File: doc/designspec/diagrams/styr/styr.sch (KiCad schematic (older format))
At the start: 1 part

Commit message: Schematics done, need filters for sensors, some resistors for the switches etc
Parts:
- added U?: ATmega1284P-PU, Package_DIP:DIP-40_W15.24mm, symbol MCU_Microchip_ATmega:ATmega1284P-PU
- added U?: IQEXO-3, Package_SO:SOIC-8_3.9x4.9mm_P1.27mm, symbol exo3:IQEXO-3
- added U?: ADG419BN, Package_DIP:DIP-8_W7.62mm, symbol Analog_Switch:ADG419BN
- added _?: JMA162A, Display_7Segment:DA04-11SYKWA, symbol jma162a:JMA162A
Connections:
- net labels added: CHIP_SELECT, MISO, MOSI, PWM_MOTOR, PWM_SVÄNG, SPI_CLK
- wire segments 0 -> 51
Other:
- moved on the sheet: J?
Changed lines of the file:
@@
 EESchema Schematic File Version 4
+LIBS:styr-cache
 EELAYER 26 0
 EELAYER END
@@
 L Connector:AVR-JTAG-10 J?
 U 1 1 5BBCAF71
-P 2100 1350
-F 0 "J?" H 1720 1396 50  0000 R CNN
-F 1 "AVR-JTAG-10" H 1720 1305 50  0000 R CNN
-F 2 "" V 1950 1500 50  0001 C CNN
-F 3 " ~" H 825 800 50  0001 C CNN
-	1    2100 1350
+P 5050 3550
+F 0 "J?" H 4670 3596 50  0000 R CNN
+F 1 "AVR-JTAG-10" H 4670 3505 50  0000 R CNN
+F 2 "" V 4900 3700 50  0001 C CNN
+F 3 " ~" H 3775 3000 50  0001 C CNN
+	1    5050 3550
+	-1   0    0    -1
+$EndComp
+$Comp
+L MCU_Microchip_ATmega:ATmega1284P-PU U?
+U 1 1 5BEA84E2
+P 2850 3150
+F 0 "U?" H 2850 1064 50  0000 C CNN
+F 1 "ATmega1284P-PU" H 2850 973 50  0000 C CNN
+F 2 "Package_DIP:DIP-40_W15.24mm" H 2850 3150 50  0001 C CIN
+F 3 "http://ww1.microchip.com/downloads/en/DeviceDoc/Atmel-8272-8-bit-AVR-microcontroller-ATmega164A_PA-324A_PA-644A_PA-1284_P_datasheet.pdf" H 2850 3150 50  0001 C CNN
+	1    2850 3150
 	1    0    0    -1
 $EndComp
+$Comp
+L exo3:IQEXO-3 U?
+U 1 1 5BEB103D
+P 1350 2150
+F 0 "U?" H 1350 2717 50  0000 C CNN
+F 1 "IQEXO-3" H 1350 2626 50  0000 C CNN
+F 2 "Package_SO:SOIC-8_3.9x4.9mm_P1.27mm" H 1400 1400 50  0001 C CNN
+F 3 "http://www.onsemi.com/pub/Collateral/NB3N511-D.PDF" H 1400 1300 50  0001 C CNN
+	1    1350 2150
+	0    1    -1   0
+$EndComp
+$Comp
+L jma162a:JMA162A _?
+U 1 1 5BEB1179
+P 4800 6000
+F 0 "_?" V 4600 5650 50  0001 C CNN
+F 1 "JMA162A" H 4800 5425 50  0000 C CNN
+F 2 "Display_7Segment:DA04-11SYKWA" V 5975 5975 50  0001 C CNN
+F 3 "http://www.kingbright.com/attachments/file/psearch/000/00/00/DA04-11SYKWA(Ver.6A).pdf" V 4600 6420 50  0001 C CNN
+	1    4800 6000
+	0    1    -1   0
+$EndComp
+$Comp
+L Analog_Switch:ADG419BN U?
+U 1 1 5BEB1382
+P 1950 1250
+F 0 "U?" H 1950 1492 50  0000 C CNN
+F 1 "ADG419BN" H 1950 1401 50  0000 C CNN
+F 2 "Package_DIP:DIP-8_W7.62mm" H 1950 950 50  0001 C CNN
+F 3 "http://www.analog.com/media/en/technical-documentation/data-sheets/ADG419.pdf" H 1950 1050 50  0001 C CNN
+	1    1950 1250
+	1    0    0    -1
+$EndComp
+Wire Wire Line
+	1150 1750 1150 900
+Wire Wire Line
+	1150 900  2850 900
+Wire Wire Line
+	2850 900  2850 1150
+Wire Wire Line
+	1650 2550 2100 2550
+Wire Wire Line
+	2100 2550 2100 1650
+Wire Wire Line
+	2100 1650 2250 1650
+Wire Wire Line
+	1150 5150 2850 5150
+Connection ~ 2850 900
+Wire Wire Line
+	2850 900  5050 900
+Wire Wire Line
+	5050 900  7600 900
+Connection ~ 5050 900
+Wire Wire Line
+	4450 5300 4100 5300
+Wire Wire Line
+	4100 5300 4100 3950
+Wire Wire Line
+	4100 3950 3450 3950
+Wire Wire Line
+	4550 5300 4550 4850
+Wire Wire Line
+	4550 4850 3450 4850
+Wire Wire Line
+	4650 5300 4650 4750
+Wire Wire Line
+	4650 4750 3450 4750
+Wire Wire Line
+	4750 5300 4750 4650
+Wire Wire Line
+	4750 4650 3450 4650
+Wire Wire Line
+	3450 4550 4850 4550
+Wire Wire Line
+	4850 4550 4850 5300
+Wire Wire Line
+	3450 4450 4950 4450
+Wire Wire Line
+	4950 4450 4950 5300
+Wire Wire Line
+	5050 5300 5050 4350
+Wire Wire Line
+	5050 4350 3450 4350
+Wire Wire Line
+	3450 4250 5150 4250
+Wire Wire Line
+	5150 4250 5150 5300
+Wire Wire Line
+	5250 5300 5250 4200
+Wire Wire Line
+	5400 6250 7600 6250
+Wire Wire Line
+	7600 900  7600 6250
+Wire Wire Line
+	4450 6700 5850 6700
+Wire Wire Line
+	2850 5150 2850 6700
+Wire Wire Line
+	2850 6700 4450 6700
+Connection ~ 2850 5150
+Connection ~ 4450 6700
+Wire Wire Line
+	4550 3750 3450 3750
+Wire Wire Line
+	2950 1150 5150 1150
+Wire Wire Line
+	1150 2500 1150 5150
+Wire Wire Line
+	3450 3650 4550 3650
+Wire Wire Line
+	3450 3550 4550 3550
+Wire Wire Line
+	3450 3450 4550 3450
+Wire Wire Line
+	4950 4150 4950 4200
+Wire Wire Line
+	4950 4200 5250 4200
+Wire Wire Line
+	3450 4150 4950 4150
+Wire Wire Line
+	5850 4150 5850 6700
+Wire Wire Line
+	5050 4150 5850 4150
+Wire Wire Line
+	5050 900  5050 2950
+Wire Wire Line
+	5150 1150 5150 2950
+Wire Wire Line
+	3450 3050 4150 3050
+Wire Wire Line
+	3450 2950 4150 2950
+Wire Wire Line
+	3450 2850 4150 2850
+Wire Wire Line
+	3450 2750 4150 2750
+Text Label 4150 3050 0    50   ~ 0
+SPI_CLK
+Text Label 4150 2950 0    50   ~ 0
+MISO
+Text Label 4150 2850 0    50   ~ 0
+MOSI
+Text Label 4150 2750 0    50   ~ 0
+CHIP_SELECT
+Wire Wire Line
+	3450 2650 4150 2650
+Wire Wire Line
+	3450 2550 4150 2550
+Text Label 4150 2650 0    50   ~ 0
+PWM_MOTOR
+Text Label 4150 2550 0    50   ~ 0
+PWM_SVÄNG
 $EndSCHEMATC

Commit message: Forgot that there were 2 halleffektsensors, changed the pins since OC pins are set to specified ports which i needed to free
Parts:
- removed _?: JMA162A, Display_7Segment:DA04-11SYKWA, symbol jma162a:JMA162A
- added _?: JMA162A, Display_7Segment:DA04-11SYKWA, symbol jma162a:JMA162A
- U?: value IQEXO-3 -> OSCILLATOR-QEXO3
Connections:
- net labels added: GNDREF
- wire segments 51 -> 44
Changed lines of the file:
@@
 P 1350 2150
 F 0 "U?" H 1350 2717 50  0000 C CNN
-F 1 "IQEXO-3" H 1350 2626 50  0000 C CNN
+F 1 "OSCILLATOR-QEXO3" H 1350 2626 50  0000 C CNN
 F 2 "Package_SO:SOIC-8_3.9x4.9mm_P1.27mm" H 1400 1400 50  0001 C CNN
 F 3 "http://www.onsemi.com/pub/Collateral/NB3N511-D.PDF" H 1400 1300 50  0001 C CNN
 	1    1350 2150
-	0    1    -1   0
-$EndComp
-$Comp
-L jma162a:JMA162A _?
-U 1 1 5BEB1179
-P 4800 6000
-F 0 "_?" V 4600 5650 50  0001 C CNN
-F 1 "JMA162A" H 4800 5425 50  0000 C CNN
-F 2 "Display_7Segment:DA04-11SYKWA" V 5975 5975 50  0001 C CNN
-F 3 "http://www.kingbright.com/attachments/file/psearch/000/00/00/DA04-11SYKWA(Ver.6A).pdf" V 4600 6420 50  0001 C CNN
-	1    4800 6000
 	0    1    -1   0
 $EndComp
@@
 Connection ~ 5050 900
 Wire Wire Line
-	4450 5300 4100 5300
-Wire Wire Line
-	4100 5300 4100 3950
-Wire Wire Line
-	4100 3950 3450 3950
-Wire Wire Line
-	4550 5300 4550 4850
-Wire Wire Line
-	4550 4850 3450 4850
-Wire Wire Line
-	4650 5300 4650 4750
-Wire Wire Line
-	4650 4750 3450 4750
-Wire Wire Line
-	4750 5300 4750 4650
-Wire Wire Line
-	4750 4650 3450 4650
-Wire Wire Line
-	3450 4550 4850 4550
-Wire Wire Line
-	4850 4550 4850 5300
-Wire Wire Line
-	3450 4450 4950 4450
-Wire Wire Line
-	4950 4450 4950 5300
-Wire Wire Line
-	5050 5300 5050 4350
-Wire Wire Line
-	5050 4350 3450 4350
-Wire Wire Line
-	3450 4250 5150 4250
-Wire Wire Line
-	5150 4250 5150 5300
-Wire Wire Line
-	5250 5300 5250 4200
-Wire Wire Line
-	5400 6250 7600 6250
-Wire Wire Line
-	7600 900  7600 6250
-Wire Wire Line
-	4450 6700 5850 6700
-Wire Wire Line
-	2850 5150 2850 6700
-Wire Wire Line
-	2850 6700 4450 6700
-Connection ~ 2850 5150
-Connection ~ 4450 6700
+	7600 900  7600 3500
 Wire Wire Line
 	4550 3750 3450 3750
@@
 Wire Wire Line
 	3450 3450 4550 3450
-Wire Wire Line
-	4950 4150 4950 4200
-Wire Wire Line
-	4950 4200 5250 4200
-Wire Wire Line
-	3450 4150 4950 4150
-Wire Wire Line
-	5850 4150 5850 6700
-Wire Wire Line
-	5050 4150 5850 4150
 Wire Wire Line
 	5050 900  5050 2950
@@
 Wire Wire Line
 	3450 2650 4150 2650
-Wire Wire Line
-	3450 2550 4150 2550
 Text Label 4150 2650 0    50   ~ 0
 PWM_MOTOR
-Text Label 4150 2550 0    50   ~ 0
+$Comp
+L jma162a:JMA162A _?
+U 1 1 5BEDF369
+P 6650 3250
+F 0 "_?" V 6450 2900 50  0001 C CNN
+F 1 "JMA162A" H 6650 2675 50  0000 C CNN
+F 2 "Display_7Segment:DA04-11SYKWA" V 7825 3225 50  0001 C CNN
+F 3 "http://www.kingbright.com/attachments/file/psearch/000/00/00/DA04-11SYKWA(Ver.6A).pdf" V 6450 3670 50  0001 C CNN
+	1    6650 3250
+	0    1    -1   0
+$EndComp
+Wire Wire Line
+	6400 2550 6400 2150
+Wire Wire Line
+	6400 2150 3450 2150
+Wire Wire Line
+	6500 2550 6500 2050
+Wire Wire Line
+	6500 2050 3450 2050
+Wire Wire Line
+	6600 2550 6600 1950
+Wire Wire Line
+	6600 1950 3450 1950
+Wire Wire Line
+	6700 2550 6700 1850
+Wire Wire Line
+	6700 1850 3450 1850
+Wire Wire Line
+	6800 2550 6800 1750
+Wire Wire Line
+	6800 1750 3450 1750
+Wire Wire Line
+	6900 2550 6900 1650
+Wire Wire Line
+	6900 1650 3450 1650
+Wire Wire Line
+	3450 1550 7000 1550
+Wire Wire Line
+	7000 1550 7000 2550
+Wire Wire Line
+	7100 2550 7100 1450
+Wire Wire Line
+	7100 1450 3450 1450
+Wire Wire Line
+	3450 2350 6300 2350
+Wire Wire Line
+	6300 2350 6300 2550
+Wire Wire Line
+	3450 4650 4150 4650
+Text Label 4150 4650 0    50   ~ 0
 PWM_SVÄNG
+Wire Wire Line
+	7250 3500 7600 3500
+Connection ~ 7600 3500
+Wire Wire Line
+	7600 3500 7600 6250
+$Comp
+L power:GNDREF #PWR?
+U 1 1 5BEEFE97
+P 6300 3950
+F 0 "#PWR?" H 6300 3700 50  0001 C CNN
+F 1 "GNDREF" H 6305 3777 50  0000 C CNN
+F 2 "" H 6300 3950 50  0001 C CNN
+F 3 "" H 6300 3950 50  0001 C CNN
+	1    6300 3950
+	1    0    0    -1
+$EndComp
+$Comp
+L power:GNDREF #PWR?
+U 1 1 5BEEFEC1
+P 5050 4150
+F 0 "#PWR?" H 5050 3900 50  0001 C CNN
+F 1 "GNDREF" H 5055 3977 50  0000 C CNN
+F 2 "" H 5050 4150 50  0001 C CNN
+F 3 "" H 5050 4150 50  0001 C CNN
+	1    5050 4150
+	1    0    0    -1
+$EndComp
 $EndSCHEMATC

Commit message: final stage of schematics first assignment
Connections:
- net labels added: +5V
- wire segments 44 -> 36
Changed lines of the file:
@@
 Sheet 1 1
 Title "Styrmodul"
-Date "2018-10-09"
+Date "2018-11-06"
 Rev ""
 Comp ""
@@
 $EndComp
 Wire Wire Line
-	1150 1750 1150 900
-Wire Wire Line
-	1150 900  2850 900
-Wire Wire Line
-	2850 900  2850 1150
-Wire Wire Line
 	1650 2550 2100 2550
 Wire Wire Line
@@
 	2100 1650 2250 1650
 Wire Wire Line
-	1150 5150 2850 5150
-Connection ~ 2850 900
-Wire Wire Line
-	2850 900  5050 900
-Wire Wire Line
-	5050 900  7600 900
-Connection ~ 5050 900
-Wire Wire Line
-	7600 900  7600 3500
-Wire Wire Line
 	4550 3750 3450 3750
 Wire Wire Line
-	2950 1150 5150 1150
-Wire Wire Line
-	1150 2500 1150 5150
-Wire Wire Line
 	3450 3650 4550 3650
 Wire Wire Line
@@
 Wire Wire Line
 	3450 3450 4550 3450
-Wire Wire Line
-	5050 900  5050 2950
-Wire Wire Line
-	5150 1150 5150 2950
 Wire Wire Line
 	3450 3050 4150 3050
@@
 Text Label 4150 4650 0    50   ~ 0
 PWM_SVÄNG
-Wire Wire Line
-	7250 3500 7600 3500
-Connection ~ 7600 3500
-Wire Wire Line
-	7600 3500 7600 6250
 $Comp
 L power:GNDREF #PWR?
@@
 	1    0    0    -1
 $EndComp
+$Comp
+L power:GNDREF #PWR?
+U 1 1 5BE0FDF7
+P 1150 2550
+F 0 "#PWR?" H 1150 2300 50  0001 C CNN
+F 1 "GNDREF" H 1155 2377 50  0000 C CNN
+F 2 "" H 1150 2550 50  0001 C CNN
+F 3 "" H 1150 2550 50  0001 C CNN
+	1    1150 2550
+	1    0    0    -1
+$EndComp
+$Comp
+L power:+5V #PWR?
+U 1 1 5BE10664
+P 1650 1750
+F 0 "#PWR?" H 1650 1600 50  0001 C CNN
+F 1 "+5V" H 1665 1923 50  0000 C CNN
+F 2 "" H 1650 1750 50  0001 C CNN
+F 3 "" H 1650 1750 50  0001 C CNN
+	1    1650 1750
+	1    0    0    -1
+$EndComp
+$Comp
+L power:+5V #PWR?
+U 1 1 5BE1138F
+P 7250 3500
+F 0 "#PWR?" H 7250 3350 50  0001 C CNN
+F 1 "+5V" H 7265 3673 50  0000 C CNN
+F 2 "" H 7250 3500 50  0001 C CNN
+F 3 "" H 7250 3500 50  0001 C CNN
+	1    7250 3500
+	0    1    1    0
+$EndComp
+$Comp
+L power:+5V #PWR?
+U 1 1 5BE1401A
+P 5050 2950
+F 0 "#PWR?" H 5050 2800 50  0001 C CNN
+F 1 "+5V" H 5065 3123 50  0000 C CNN
+F 2 "" H 5050 2950 50  0001 C CNN
+F 3 "" H 5050 2950 50  0001 C CNN
+	1    5050 2950
+	1    0    0    -1
+$EndComp
+$Comp
+L power:+5V #PWR?
+U 1 1 5BE1406E
+P 5150 2950
+F 0 "#PWR?" H 5150 2800 50  0001 C CNN
+F 1 "+5V" H 5165 3123 50  0000 C CNN
+F 2 "" H 5150 2950 50  0001 C CNN
+F 3 "" H 5150 2950 50  0001 C CNN
+	1    5150 2950
+	1    0    0    -1
+$EndComp
+$Comp
+L power:GNDREF #PWR?
+U 1 1 5BE14189
+P 3350 5150
+F 0 "#PWR?" H 3350 4900 50  0001 C CNN
+F 1 "GNDREF" H 3355 4977 50  0000 C CNN
+F 2 "" H 3350 5150 50  0001 C CNN
+F 3 "" H 3350 5150 50  0001 C CNN
+	1    3350 5150
+	1    0    0    -1
+$EndComp
+Wire Wire Line
+	2850 5150 3350 5150
+Wire Wire Line
+	2850 1150 2850 1000
+Wire Wire Line
+	2850 1000 2900 1000
+Wire Wire Line
+	2950 1000 2950 1150
+$Comp
+L power:+5V #PWR?
+U 1 1 5BE15085
+P 2900 1000
+F 0 "#PWR?" H 2900 850 50  0001 C CNN
+F 1 "+5V" H 2915 1173 50  0000 C CNN
+F 2 "" H 2900 1000 50  0001 C CNN
+F 3 "" H 2900 1000 50  0001 C CNN
+	1    2900 1000
+	1    0    0    -1
+$EndComp
+Connection ~ 2900 1000
+Wire Wire Line
+	2900 1000 2950 1000
 $EndSCHEMATC

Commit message: Updated reset switch for reset and styr
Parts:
- removed U?: ADG419BN, Package_DIP:DIP-8_W7.62mm, symbol Analog_Switch:ADG419BN
- added C?: _, symbol pspice:CAP
- added R?: R, symbol pspice:R
- added U?: Tryckknapp, Package_DIP:DIP-8_W7.62mm, symbol Analog_Switch:ADG417BN
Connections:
- wire segments 36 -> 41
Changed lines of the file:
@@
 	0    1    -1   0
-$EndComp
-$Comp
-L Analog_Switch:ADG419BN U?
-U 1 1 5BEB1382
-P 1950 1250
-F 0 "U?" H 1950 1492 50  0000 C CNN
-F 1 "ADG419BN" H 1950 1401 50  0000 C CNN
-F 2 "Package_DIP:DIP-8_W7.62mm" H 1950 950 50  0001 C CNN
-F 3 "http://www.analog.com/media/en/technical-documentation/data-sheets/ADG419.pdf" H 1950 1050 50  0001 C CNN
-	1    1950 1250
-	1    0    0    -1
 $EndComp
 Wire Wire Line
@@
 Wire Wire Line
 	2900 1000 2950 1000
+$Comp
+L Analog_Switch:ADG417BN U?
+U 1 1 5BE2F395
+P 950 1150
+F 0 "U?" H 950 1417 50  0000 C CNN
+F 1 "Tryckknapp" H 950 1326 50  0000 C CNN
+F 2 "Package_DIP:DIP-8_W7.62mm" H 950 1050 50  0001 C CNN
+F 3 "http://www.analog.com/media/en/technical-documentation/data-sheets/ADG417.pdf" H 950 1150 50  0001 C CNN
+	1    950  1150
+	1    0    0    -1
+$EndComp
+$Comp
+L pspice:CAP C?
+U 1 1 5BE2FC49
+P 950 1600
+F 0 "C?" V 1231 1600 8   0000 C CNN
+F 1 "_" V 1174 1600 50  0000 C CNN
+F 2 "" H 950 1600 50  0001 C CNN
+F 3 "" H 950 1600 50  0001 C CNN
+	1    950  1600
+	0    -1   -1   0
+$EndComp
+$Comp
+L pspice:R R?
+U 1 1 5BE3264E
+P 1000 750
+F 0 "R?" V 795 750 50  0000 C CNN
+F 1 "R" V 886 750 50  0000 C CNN
+F 2 "" H 1000 750 50  0001 C CNN
+F 3 "" H 1000 750 50  0001 C CNN
+	1    1000 750
+	0    1    1    0
+$EndComp
+Wire Wire Line
+	1250 750  1250 1150
+Connection ~ 1250 1150
+Wire Wire Line
+	1250 1150 2250 1150
+Wire Wire Line
+	2250 1150 2250 1450
+$Comp
+L power:GNDREF #PWR?
+U 1 1 5BE34C2C
+P 650 1150
+F 0 "#PWR?" H 650 900 50  0001 C CNN
+F 1 "GNDREF" H 655 977 50  0000 C CNN
+F 2 "" H 650 1150 50  0001 C CNN
+F 3 "" H 650 1150 50  0001 C CNN
+	1    650  1150
+	1    0    0    -1
+$EndComp
+$Comp
+L power:GNDREF #PWR?
+U 1 1 5BE34C68
+P 700 1600
+F 0 "#PWR?" H 700 1350 50  0001 C CNN
+F 1 "GNDREF" H 705 1427 50  0000 C CNN
+F 2 "" H 700 1600 50  0001 C CNN
+F 3 "" H 700 1600 50  0001 C CNN
+	1    700  1600
+	1    0    0    -1
+$EndComp
+$Comp
+L power:+5V #PWR?
+U 1 1 5BE34CC7
+P 750 750
+F 0 "#PWR?" H 750 600 50  0001 C CNN
+F 1 "+5V" V 765 878 50  0000 L CNN
+F 2 "" H 750 750 50  0001 C CNN
+F 3 "" H 750 750 50  0001 C CNN
+	1    750  750
+	0    -1   -1   0
+$EndComp
+Wire Wire Line
+	1200 1600 1250 1600
+Wire Wire Line
+	1250 1150 1250 1600
 $EndSCHEMATC

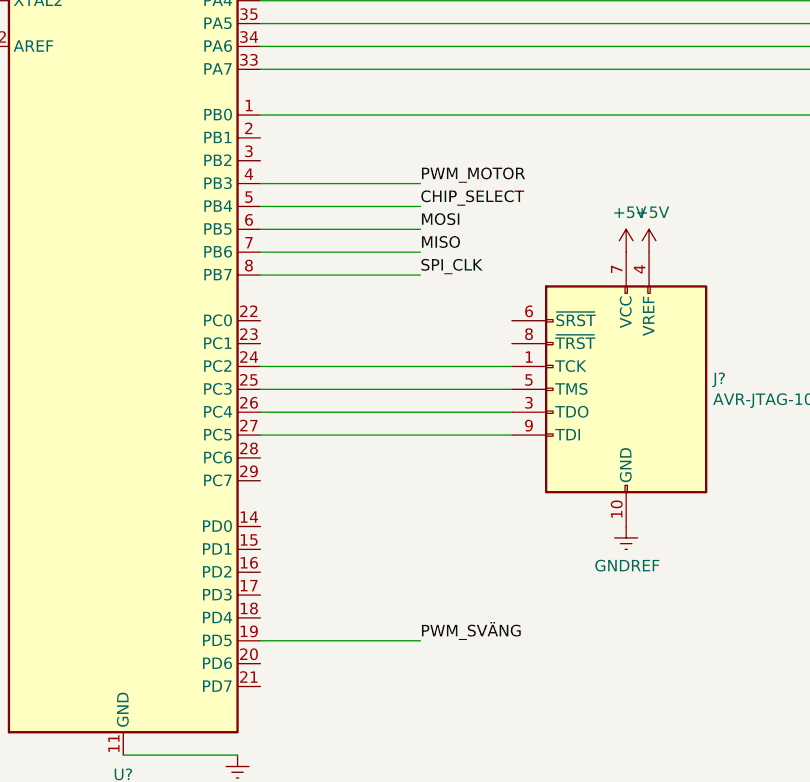
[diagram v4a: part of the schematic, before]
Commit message: Added LP-filters between sensors
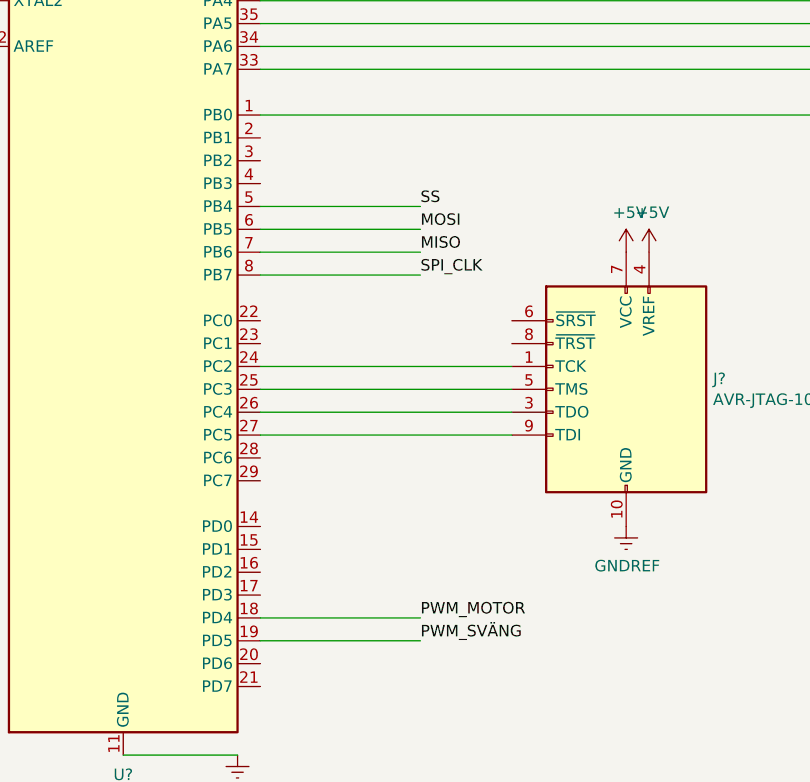
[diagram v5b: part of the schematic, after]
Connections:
- net labels added: SS
- net labels removed: CHIP_SELECT
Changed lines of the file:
@@
 MOSI
 Text Label 4150 2750 0    50   ~ 0
-CHIP_SELECT
-Wire Wire Line
-	3450 2650 4150 2650
-Text Label 4150 2650 0    50   ~ 0
-PWM_MOTOR
+SS
 $Comp
 L jma162a:JMA162A _?
@@
 Wire Wire Line
 	1250 1150 1250 1600
+Wire Wire Line
+	3450 4550 4150 4550
+Text Label 4150 4550 0    50   ~ 0
+PWM_MOTOR
 $EndSCHEMATC
